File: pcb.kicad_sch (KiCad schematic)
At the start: 31 parts, among them J1 Raspberry_Pi_2_3, J10 Conn_01x03_Male, J2 Conn_01x03_Male, J3 Conn_01x03_Male, J4 Conn_01x02_Male, J5 Conn_01x02_Male, J6 Conn_01x03_Male, J7 Conn_01x05_Male, J8 Conn_01x03_Male, J9 Conn_01x03_Male, U1 TPS54xxxDDA, U3 PCA9685PW

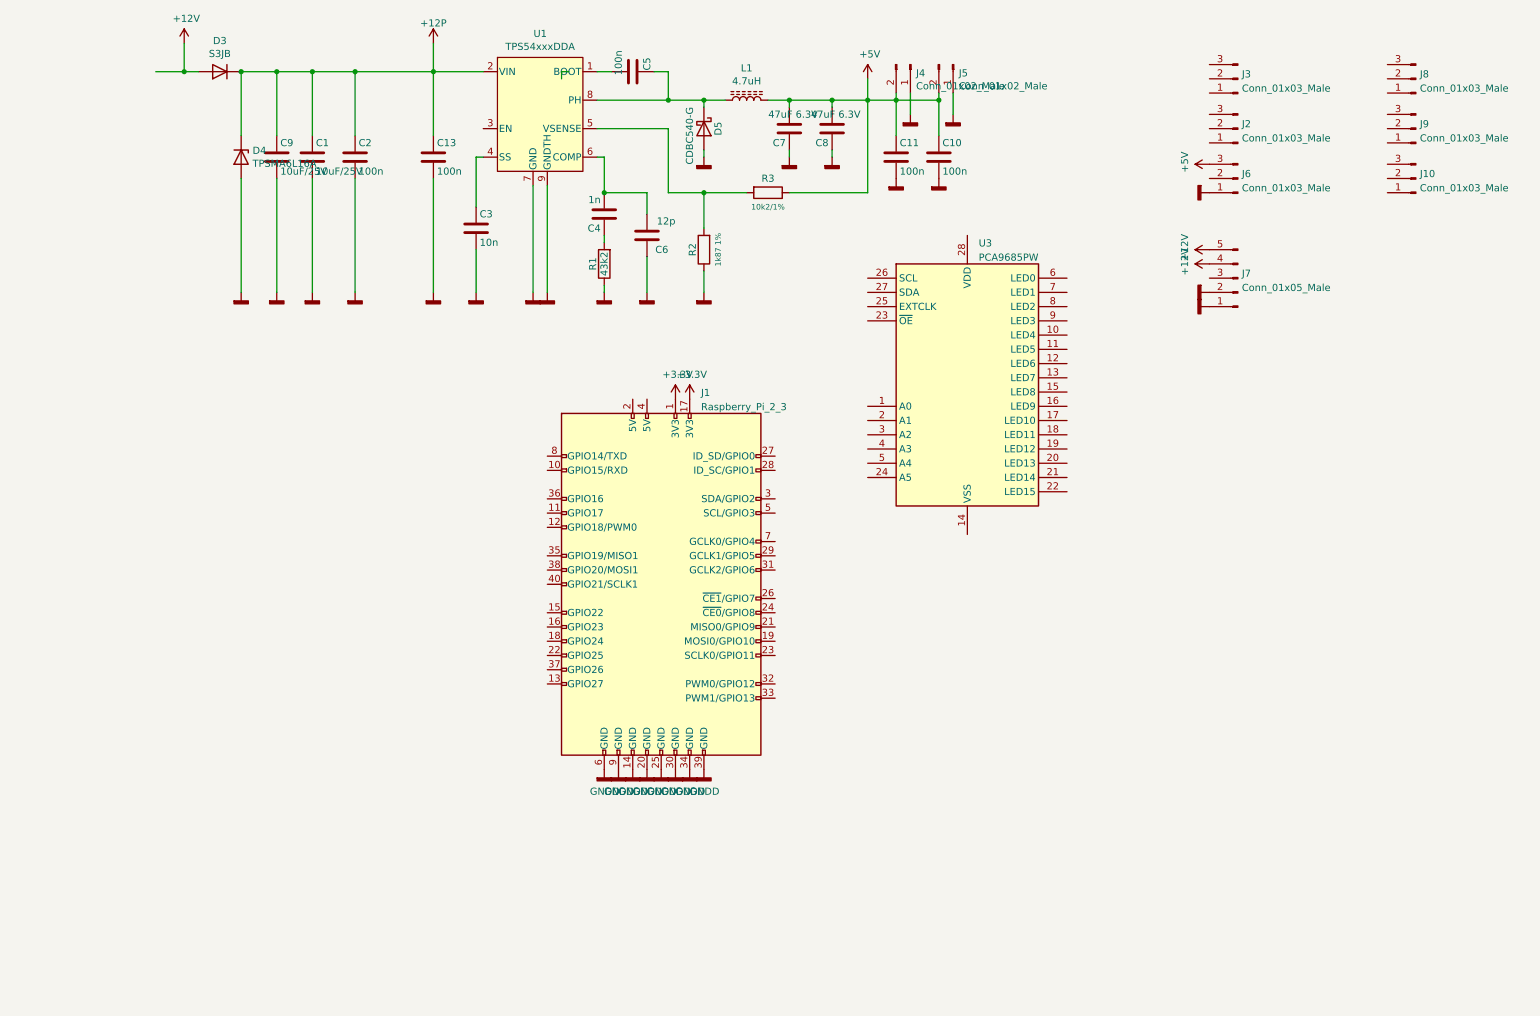
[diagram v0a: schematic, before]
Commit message: added images & plug placement
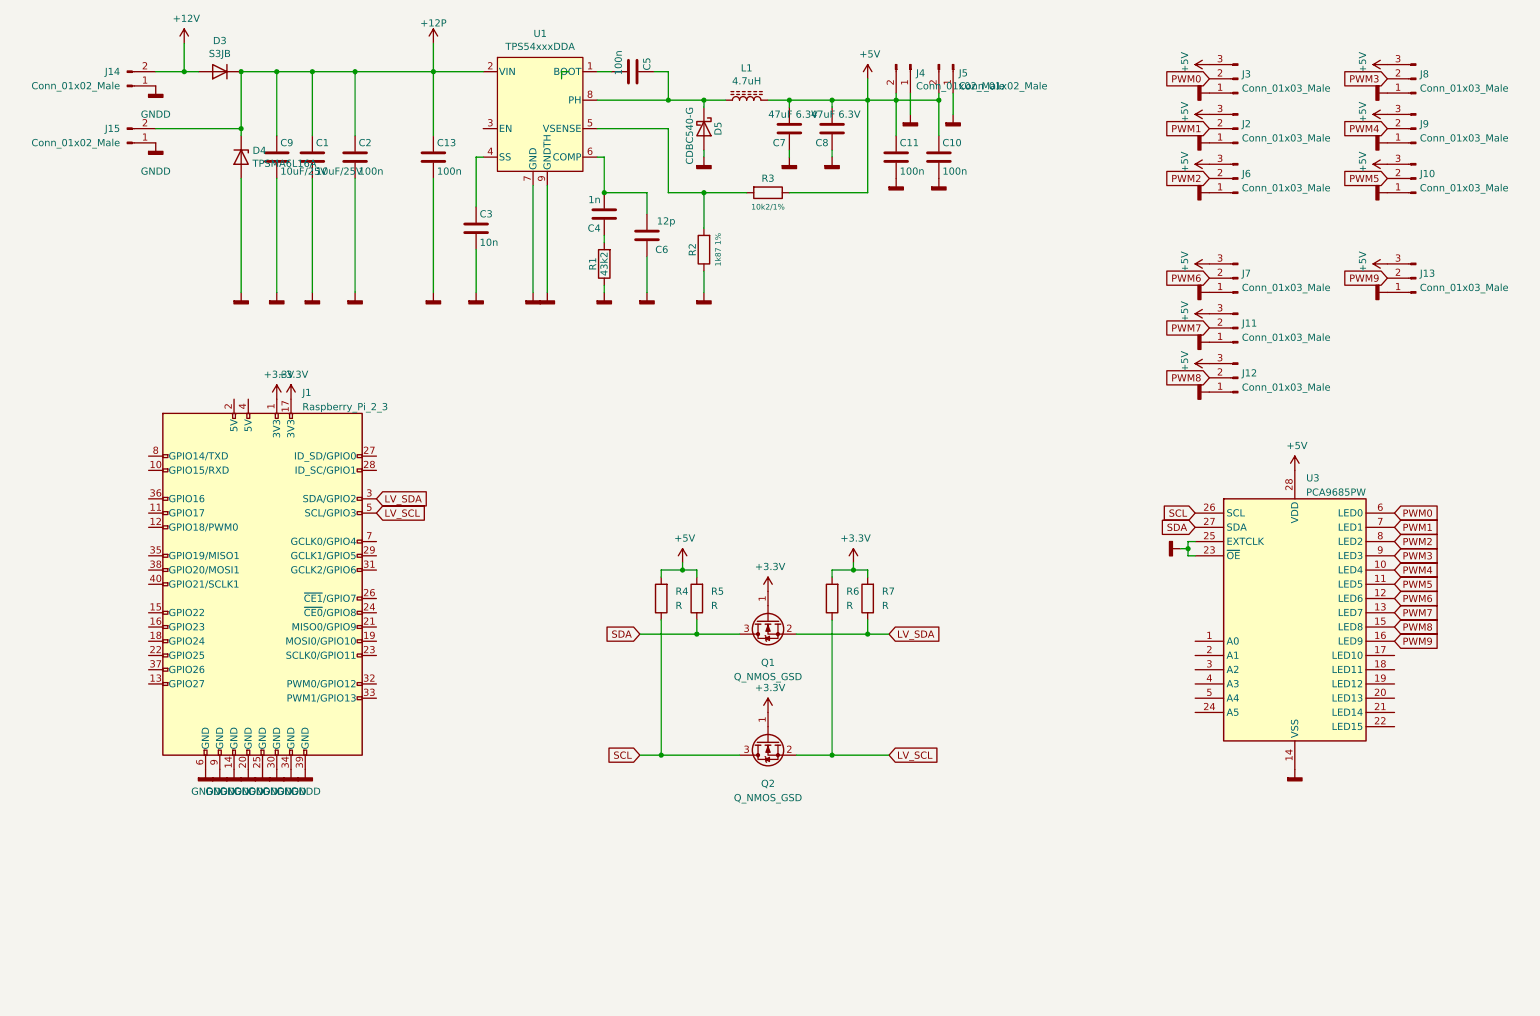
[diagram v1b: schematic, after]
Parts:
- removed J7: Conn_01x05_Male, MyKiCAD:Molex_1x05x2.54mm_Angled, symbol Connector:Conn_01x05_Male
- added J11, J12, J13, J7: Conn_01x03_Male, Connector_JST:JST_XH_B3B-XH-A_1x03_P2.50mm_Vertical, symbol Connector:Conn_01x03_Male
- added J14, J15: Conn_01x02_Male, Connector_JST:JST_XH_S2B-XH-A_1x02_P2.50mm_Horizontal, symbol Connector:Conn_01x02_Male
- added Q1, Q2: Q_NMOS_GSD, Package_TO_SOT_SMD:SOT-23, symbol Device:Q_NMOS_GSD
- added R4, R5, R6, R7: R, Resistor_SMD:R_0603_1608Metric, symbol Device:R
- J4, J5: footprint Connector_JST:JST_XH_B2B-XH-A_1x02_P2.50mm_Vertical -> Connector_JST:JST_XH_S2B-XH-A_1x02_P2.50mm_Horizontal
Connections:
- net +12P: now also J15.2 (Pin_2)
- net +12V: now also J14.2 (Pin_2)
- net +3.3V: now also Q1.1 (G), Q2.1 (G), R6.2, R7.2
- net +5V: now also J10.3 (Pin_3), J2.3 (Pin_3), J3.3 (Pin_3), J8.3 (Pin_3), J9.3 (Pin_3), U3.28 (VDD), J11.3 (Pin_3), J12.3 (Pin_3), J13.3 (Pin_3), J7.3 (Pin_3), R4.2, R5.2
- net GNDD: now also J10.1 (Pin_1), J2.1 (Pin_1), J3.1 (Pin_1), J8.1 (Pin_1), J9.1 (Pin_1), U3.14 (VSS), U3.23 (~{OE}), U3.25 (EXTCLK), J11.1 (Pin_1), J12.1 (Pin_1), J13.1 (Pin_1), J14.1 (Pin_1), J15.1 (Pin_1), J7.1 (Pin_1)
- net PWM4: now reaches U3.10 (LED4)
- net PWM4: now also J9.2 (Pin_2)
- net PWM5: now reaches U3.11 (LED5)
- net PWM5: now also J10.2 (Pin_2)
- net PWM6: now reaches U3.12 (LED6)
- net PWM6: now also J7.2 (Pin_2)
- net PWM7: now reaches U3.13 (LED7)
- net PWM7: now also J11.2 (Pin_2)
- net PWM8: now reaches U3.15 (LED8)
- net PWM8: now also J12.2 (Pin_2)
- net PWM9: now reaches U3.16 (LED9)
- net PWM9: now also J13.2 (Pin_2)
- net SCL: now reaches U3.26 (SCL)
- net SCL: now also Q2.3 (D), R4.1
- net SDA: now reaches U3.27 (SDA)
- net SDA: now also Q1.3 (D), R5.1
- net PWM0: now reaches U3.6 (LED0)
- net PWM0: now also J3.2 (Pin_2)
- net PWM1: now reaches U3.7 (LED1)
- net PWM1: now also J2.2 (Pin_2)
- net PWM2: now reaches U3.8 (LED2)
- net PWM2: now also J6.2 (Pin_2)
- net PWM3: now reaches U3.9 (LED3)
- net PWM3: now also J8.2 (Pin_2)
- net LV_SDA: now reaches J1.3 (SDA/GPIO2)
- net LV_SDA: now also Q1.2 (S), R7.1
- net LV_SCL: now reaches J1.5 (SCL/GPIO3)
- net LV_SCL: now also Q2.2 (S), R6.1
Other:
- moved on the sheet: J1, U3

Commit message: added reverse current protection
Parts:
- added Q3, Q5: MMBT3906, Package_TO_SOT_SMD:SOT-23, symbol Transistor_BJT:MMBT3906
- added Q4: Q_PMOS_GSD, Package_TO_SOT_SMD:SOT-23, symbol Device:Q_PMOS_GSD
- added R8: 10K, Resistor_SMD:R_0603_1608Metric, symbol Device:R
- added R9: 47K, Resistor_SMD:R_0603_1608Metric, symbol Device:R
- R4, R5, R6, R7: value R -> 10K
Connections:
- net +5V: now also Q3.2 (E), Q4.3 (D); no longer J10.3 (Pin_3), J11.3 (Pin_3), J12.3 (Pin_3), J13.3 (Pin_3), J2.3 (Pin_3), J3.3 (Pin_3), J6.3 (Pin_3), J7.3 (Pin_3), J8.3 (Pin_3), J9.3 (Pin_3)
- net GNDD: now also R8.2, R9.2
- new net: Q4.1 (G), Q5.2 (E), R9.1
- new net: Q3.1 (B), Q3.3 (C), Q5.1 (B), R8.1
- new net SERVO: J10.3 (Pin_3), J11.3 (Pin_3), J12.3 (Pin_3), J13.3 (Pin_3), J2.3 (Pin_3), J3.3 (Pin_3), J6.3 (Pin_3), J7.3 (Pin_3), J8.3 (Pin_3), J9.3 (Pin_3), Q4.2 (S), Q5.3 (C)
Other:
- moved on the sheet: Q1, Q2, R4, R5, R6, R7

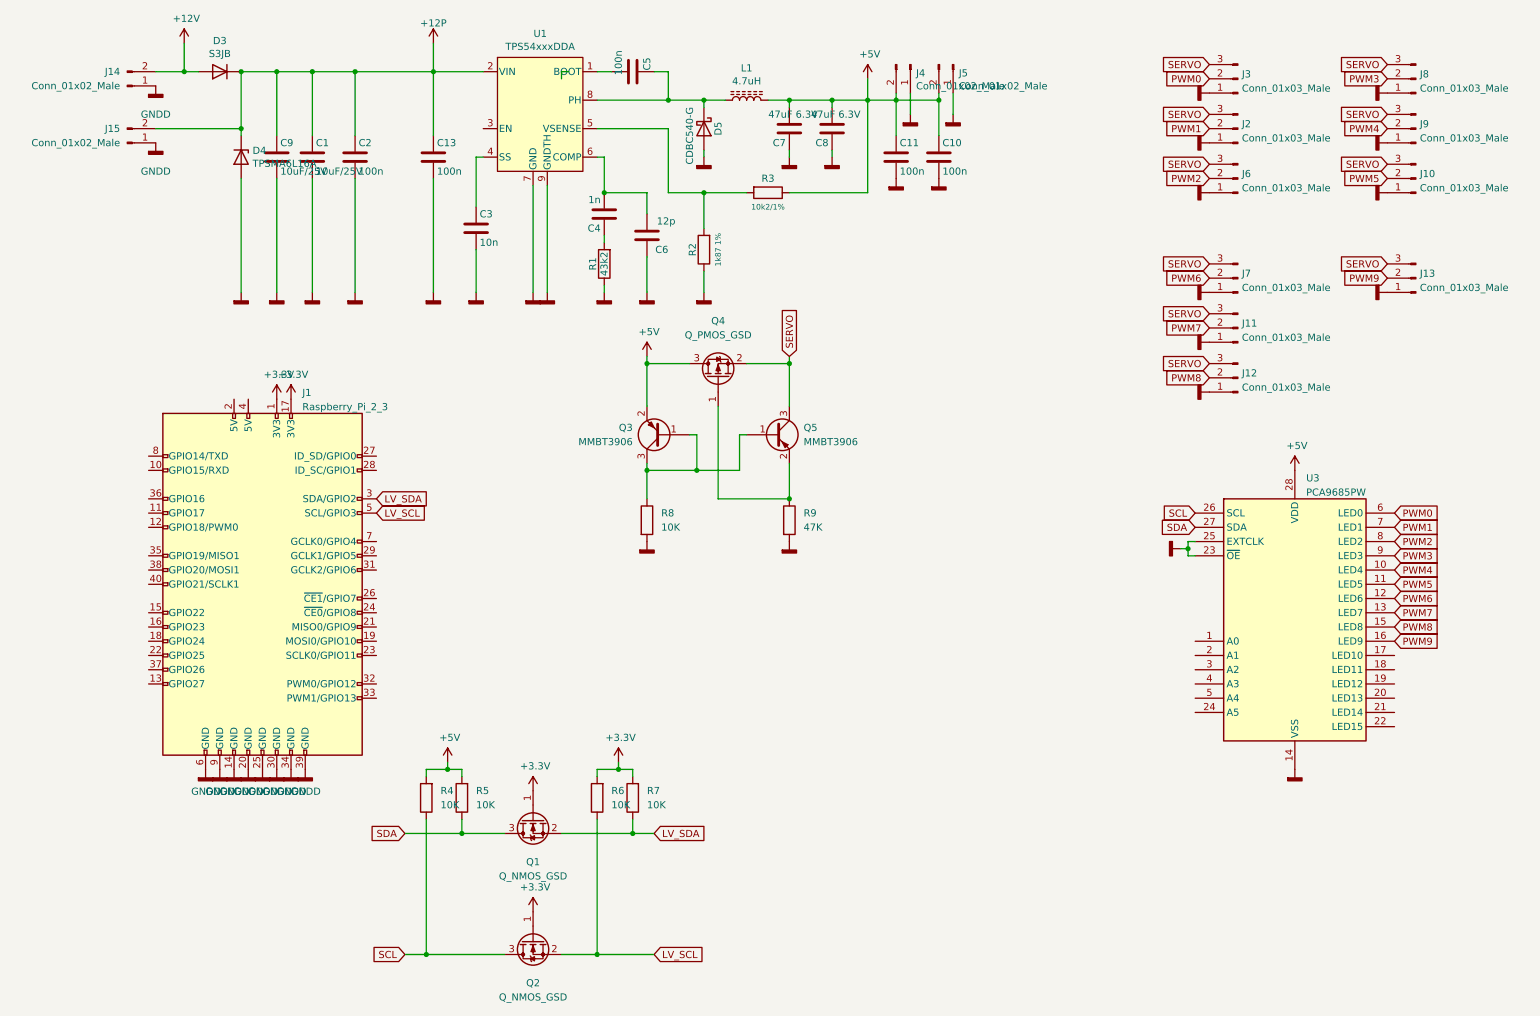
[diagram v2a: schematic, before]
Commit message: FInalized layout
DRC checked
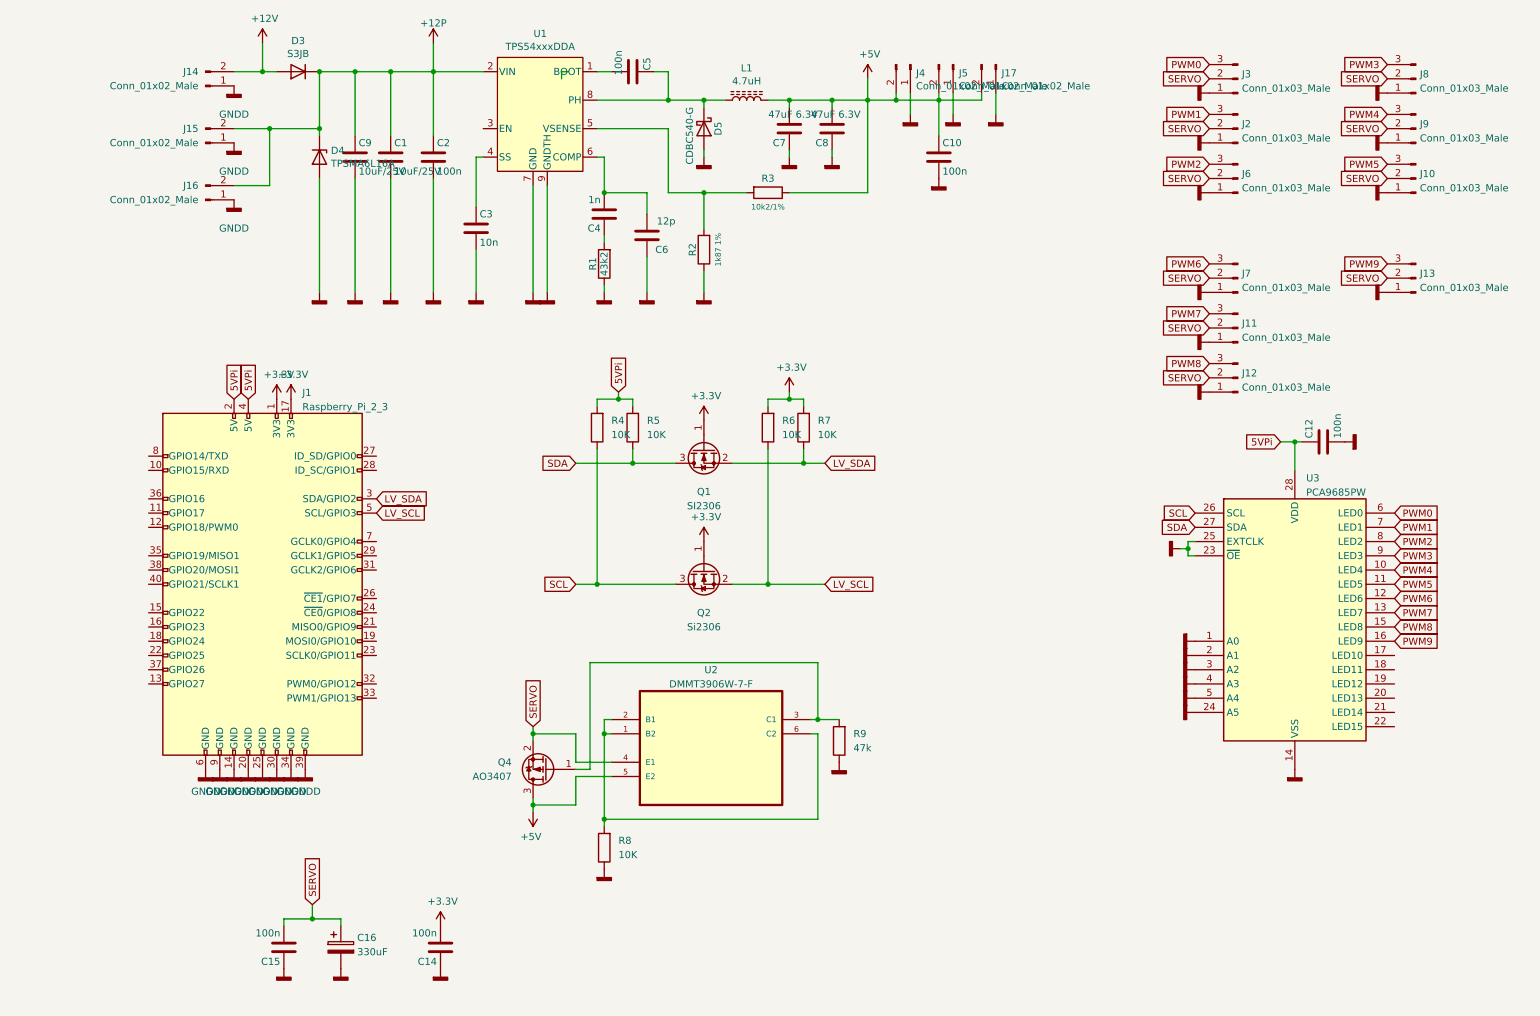
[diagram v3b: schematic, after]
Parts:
- removed C11, C13: 100n, Capacitor_SMD:C_0603_1608Metric, symbol Device:C
- removed Q3, Q5: MMBT3906, Package_TO_SOT_SMD:SOT-23, symbol Transistor_BJT:MMBT3906
- added C12, C14, C15: 100n, Capacitor_SMD:C_0603_1608Metric, symbol Device:C
- added C16: 330uF, Capacitor_THT:CP_Radial_D10.0mm_P5.00mm, symbol Device:C_Polarized
- added J16, J17: Conn_01x02_Male, Connector_JST:JST_XH_B2B-XH-A_1x02_P2.50mm_Vertical, symbol Connector:Conn_01x02_Male
- added U2: DMMT3906W-7-F, Package_TO_SOT_SMD:SOT-363_SC-70-6, symbol My_Lib:DMMT3906W-7-F
- J14, J15, J4, J5: footprint Connector_JST:JST_XH_S2B-XH-A_1x02_P2.50mm_Horizontal -> Connector_JST:JST_XH_B2B-XH-A_1x02_P2.50mm_Vertical
- Q1: value Q_NMOS_GSD -> SI2306
- Q2: value Q_NMOS_GSD -> Si2306
- Q4: value Q_PMOS_GSD -> AO3407
- R9: value 47K -> 47k
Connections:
- net +12P: now also J16.2 (Pin_2)
- net +3.3V: now also C14.2
- net +5V: now also J17.2 (Pin_2), U2.5 (E2); no longer R4.2, R5.2, U3.28 (VDD)
- net GNDD: now also R8.1, R9.1, U3.1 (A0), U3.2 (A1), U3.24 (A5), U3.3 (A2), U3.4 (A3), U3.5 (A4), C12.2, C14.1, C15.1, C16.2, J16.1 (Pin_1), J17.1 (Pin_1); no longer R8.2, R9.2
- net PWM0: now also J3.3 (Pin_3); no longer J3.2 (Pin_2)
- net PWM1: now also J2.3 (Pin_3); no longer J2.2 (Pin_2)
- net PWM2: now also J6.3 (Pin_3); no longer J6.2 (Pin_2)
- net PWM3: now also J8.3 (Pin_3); no longer J8.2 (Pin_2)
- net PWM4: now also J9.3 (Pin_3); no longer J9.2 (Pin_2)
- net PWM5: now also J10.3 (Pin_3); no longer J10.2 (Pin_2)
- net PWM6: now also J7.3 (Pin_3); no longer J7.2 (Pin_2)
- net PWM7: now also J11.3 (Pin_3); no longer J11.2 (Pin_2)
- net PWM8: now also J12.3 (Pin_3); no longer J12.2 (Pin_2)
- net PWM9: now also J13.3 (Pin_3); no longer J13.2 (Pin_2)
- net SERVO: now also J10.2 (Pin_2), J11.2 (Pin_2), J12.2 (Pin_2), J13.2 (Pin_2), J2.2 (Pin_2), J3.2 (Pin_2), J6.2 (Pin_2), J7.2 (Pin_2), J8.2 (Pin_2), J9.2 (Pin_2), C15.2, C16.1, U2.4 (E1); no longer J10.3 (Pin_3), J11.3 (Pin_3), J12.3 (Pin_3), J13.3 (Pin_3), J2.3 (Pin_3), J3.3 (Pin_3), J6.3 (Pin_3), J7.3 (Pin_3), J8.3 (Pin_3), J9.3 (Pin_3)
- net at Q4.1 (G): now also R9.2, U2.3 (C1); no longer R9.1
- net 5VPi: now reaches J1.2 (5V)
- net 5VPi: now also J1.4 (5V), R4.2, R5.2, U3.28 (VDD), C12.1
- new net: R8.2, U2.1 (B2), U2.2 (B1), U2.6 (C2)
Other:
- moved on the sheet: C1, C2, C9, D3, D4, J14, J15, Q1, Q2, R4, R5, R6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

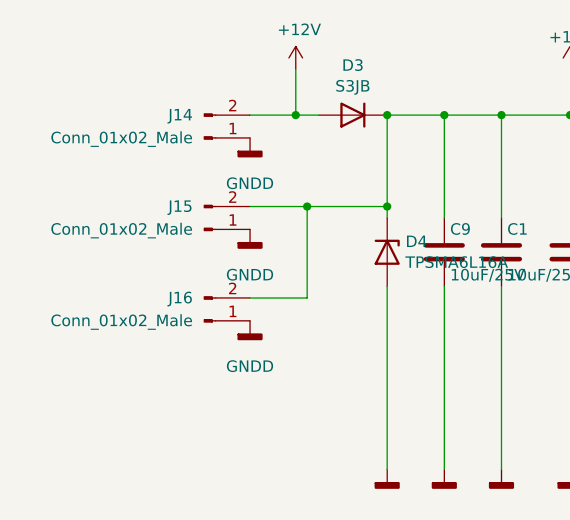
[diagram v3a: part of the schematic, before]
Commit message: Added slit for ribbon cable from pi camera
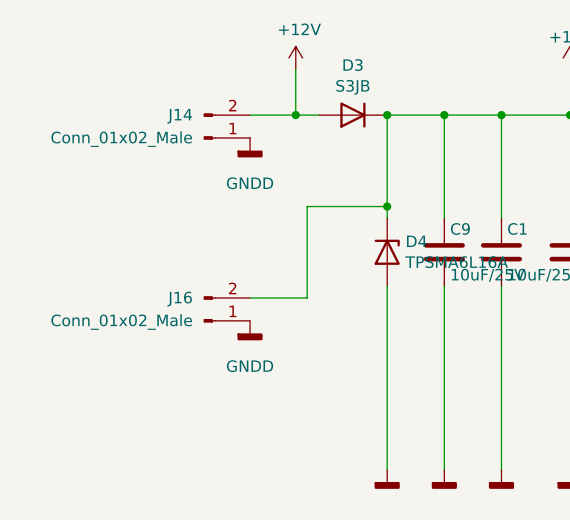
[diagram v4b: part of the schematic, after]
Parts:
- removed J15: Conn_01x02_Male, Connector_JST:JST_XH_B2B-XH-A_1x02_P2.50mm_Vertical, symbol Connector:Conn_01x02_Male
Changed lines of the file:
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@@
   (junction (at 110.49 48.26) (diameter 0) (color 0 0 0 0)
   )
-  (junction (at 50.8 36.83) (diameter 0) (color 0 0 0 0)
-  )
   (junction (at 143.51 31.75) (diameter 0) (color 0 0 0 0)
   )
@@
   )
   (wire (pts (xy 214.63 110.49) (xy 214.63 111.76))
-    (stroke (width 0) (type default) (color 0 0 0 0))
-  )
-  (wire (pts (xy 44.45 36.83) (xy 50.8 36.83))
     (stroke (width 0) (type default) (color 0 0 0 0))
   )
@@
     (pin "1")
   )
-  (symbol (lib_name "GNDD_1") (lib_id "power:GNDD") (at 44.45 39.37 0) (unit 1)
-    (in_bom yes) (on_board yes) (fields_autoplaced)
-    (property "Reference" "#PWR025" (id 0) (at 44.45 45.72 0)
-      (effects (font (size 1.27 1.27)) hide)
-    )
-    (property "Value" "GNDD" (id 1) (at 44.45 44.45 0))
-    (property "Footprint" "" (id 2) (at 44.45 39.37 0)
-      (effects (font (size 1.27 1.27)) hide)
-    )
-    (property "Datasheet" "" (id 3) (at 44.45 39.37 0)
-      (effects (font (size 1.27 1.27)) hide)
-    )
-    (pin "1")
-  )
   (symbol (lib_id "power:GNDD") (at 63.5 186.69 0) (unit 1)
     (in_bom yes) (on_board yes)
@@
     )
     (pin "1")
-  )
-  (symbol (lib_id "Connector:Conn_01x02_Male") (at 39.37 39.37 0) (mirror x) (unit 1)
-    (in_bom yes) (on_board yes) (fields_autoplaced)
-    (property "Reference" "J15" (id 0) (at 38.1 36.8299 0)
-      (effects (font (size 1.27 1.27)) (justify right))
-    )
-    (property "Value" "Conn_01x02_Male" (id 1) (at 38.1 39.3699 0)
-      (effects (font (size 1.27 1.27)) (justify right))
-    )
-    (property "Footprint" "Connector_JST:JST_XH_B2B-XH-A_1x02_P2.50mm_Vertical" (id 2) (at 39.37 39.37 0)
-      (effects (font (size 1.27 1.27)) hide)
-    )
-    (property "Datasheet" "~" (id 3) (at 39.37 39.37 0)
-      (effects (font (size 1.27 1.27)) hide)
-    )
-    (pin "1")
-    (pin "2")
   )
   (symbol (lib_id "Device:Q_NMOS_GSD") (at 128.27 115.57 90) (mirror x) (unit 1)
@@
       (reference "#PWR024") (unit 1) (value "GNDD") (footprint "")
     )
-    (path "/9ab52a4f-4e19-45f1-ae50-f00a954fac4e"
-      (reference "#PWR025") (unit 1) (value "GNDD") (footprint "")
-    )
     (path "/43d362e1-9459-4348-ab14-3501a2b74d02"
       (reference "#PWR026") (unit 1) (value "+5V") (footprint "")
@@
       (reference "J14") (unit 1) (value "Conn_01x02_Male") (footprint "Connector_JST:JST_XH_B2B-XH-A_1x02_P2.50mm_Vertical")
     )
-    (path "/acb33dbb-5fd4-4741-b760-4fce56c72c00"
-      (reference "J15") (unit 1) (value "Conn_01x02_Male") (footprint "Connector_JST:JST_XH_B2B-XH-A_1x02_P2.50mm_Vertical")
-    )
     (path "/4fbfd53c-8096-4a1f-9fca-c322a328c3a2"
